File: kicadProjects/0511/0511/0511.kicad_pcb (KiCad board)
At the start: 2 copper layers, 527.5 x 359.5 mm, 377 parts, among them J1 USB4120-03-C_REVA6, U5 UDA1334A_Breakout, U6 STM32F411RETx, U7 BD33HC5WEFJ-E2, Y1 32.768KHz, Y2 8MHz

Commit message: poursuite annotaion circuits rdc
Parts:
- moved MCP23017_ADD20 351.1 mm to (213.3, 251.2)
- moved B0_21_C1 268.0 mm to (162.5, 208.3)
- moved A0_20_C1 265.9 mm to (164.7, 223.5)
- moved B0_21_D1 265.9 mm to (164.8, 215.9)
- moved MCP23017_ADD21 50.1 mm to (212.7, 280.5)
- moved MCP23017_ADD22 49.7 mm to (213.7, 225.9)
- moved R131 16.2 mm to (244.3, 344.3)
- moved R132 16.2 mm to (244.3, 346.8)
- moved CR1 16.2 mm to (244.9, 341.5)
- moved B6_20_D1 15.5 mm to (176.5, 190.0)
- moved B6_20_R1 7.76 mm to (183.3, 190.0)
- renumbered C11 to A0_20_C1, D7 to A0_20_D1, R28 to A0_20_R1, R29 to A0_20_R2, C28 to A0_21_C1, D24 to A0_21_D2, R63 to A0_21_R1, R62 to A0_21_R2, C43 to A0_22_C1, D39 to A0_22_D1, R93 to A0_22_R1, R92 to A0_22_R2, A0_23 to A0_4, C10 to A1_20_C1, D6 to A1_20_D1, R26 to A1_20_R1, R27 to A1_20_R2, C27 to A1_21_C1, D23 to A1_21_D1, R61 to A1_21_R1, R60 to A1_21_R2, C42 to A1_22_C1, D38 to A1_22_D1, R91 to A1_22_R1, R90 to A1_22_R2, A1_23 to A1_4, C9 to A2_20_C1, D5 to A2_20_D1, R25 to A2_20_R1, R24 to A2_20_R2, C26 to A2_21_C1, D22 to A2_21_D1, R59 to A2_21_R1, R58 to A2_21_R2, C41 to A2_22_C1, D37 to A2_22_D1, R89 to A2_22_R1, R88 to A2_22_R2, A2_23 to A2_4, C20 to A3_20_C1, D16 to A3_20_D1, R47 to A3_20_R1, R46 to A3_20_R2, C21 to A3_21_C1, D17 to A3_21_D1, R49 to A3_21_R1, R48 to A3_21_R2, C52 to A3_22_C1, D48 to A3_22_D1, R111 to A3_22_R1, R110 to A3_22_R2, A3_23 to A3_4, C69 to A4_20_C1, D65 to A4_20_D1, R145 to A4_20_R1, R144 to A4_20_R2, C25 to A4_21_C1, D21 to A4_21_D1, R57 to A4_21_R1, R56 to A4_21_R2, C70 to A4_22_C1, D66 to A4_22_D1, R147 to A4_22_R1, R146 to A4_22_R2, A4_23 to A4_4, D3 to A5_20_D1, R21 to A5_20_R1, R20 to A5_20_R2, C23 to A5_21_C1, D19 to A5_21_D1, R53 to A5_21_R1, R52 to A5_21_R2, C39 to A5_22_C1, D35 to A5_22_D1, R85 to A5_22_R1, R84 to A5_22_R2, A5_23 to A5_4, C6 to A6_20_C1, D2 to A6_20_D1, R19 to A6_20_R1, R18 to A6_20_R2, C22 to A6_21_C1, D18 to A6_21_D1, R51 to A6_21_R1, R50 to A6_21_R2, C38 to A6_22_C1, D34 to A6_22_D1, R83 to A6_22_R1, R82 to A6_22_R2, A6_23 to A6_4, C12 to A7_20_C1, D8 to A7_20_D1, R31 to A7_20_R1, R30 to A7_20_R2, C36 to A7_21_C1, D32 to A7_21_D1, R79 to A7_21_R1, R78 to A7_21_R2, C44 to A7_22_C1, D40 to A7_22_D1, R95 to A7_22_R1, R94 to A7_22_R2, A7_23 to A7_4, C18 to B0_20_C1, D14 to B0_20_D1, R43 to B0_20_R1, R42 to B0_20_R2, C35 to B0_21_C1, D31 to B0_21_D1, R76 to B0_21_R1, R77 to B0_21_R2, C51 to B0_22_C1, D47 to B0_22_D1, R109 to B0_22_R1, R108 to B0_22_R2, B0_23 to B0_4, C17 to B1_20_C1, D13 to B1_20_D1, R41 to B1_20_R1, R40 to B1_20_R2, D30 to B1_21_D1, R75 to B1_21_R1, R74 to B1_21_R2, C50 to B1_22_C1, D46 to B1_22_D1, R107 to B1_22_R1, R106 to B1_22_R2, B1_23 to B1_4, C16 to B2_20_C1, D12 to B2_20_D1, R38 to B2_20_R1, R39 to B2_20_R2, C33 to B2_21_C1, D29 to B2_21_D1, R72 to B2_21_R1, R73 to B2_21_R2, C49 to B2_22_C1, D45 to B2_22_D1, R105 to B2_22_R1, R104 to B2_22_R2, B2_23 to B2_4, C15 to B3_20_C1, D11 to B3_20_D1, R37 to B3_20_R1, R36 to B3_20_R2, C32 to B3_21_C1, D28 to B3_21_D1, R71 to B3_21_R1, R70 to B3_21_R2, C48 to B3_22_C1, D44 to B3_22_D1, R103 to B3_22_R1, R102 to B3_22_R2, B3_23 to B3_4, C14 to B4_20_C1, D10 to B4_20_D1, R34 to B4_20_R1, R35 to B4_20_R2, C31 to B4_21_C1, D27 to B4_21_D1, R69 to B4_21_R1, R68 to B4_21_R2, C47 to B4_22_C1, D43 to B4_22_D1, R101 to B4_22_R1, R100 to B4_22_R2, B4_23 to B4_4, C13 to B5_20_C1, D9 to B5_20_D1, R33 to B5_20_R1, R32 to B5_20_R2, C30 to B5_21_C1, D26 to B5_21_D1, R67 to B5_21_R1, R66 to B5_21_R2, C46 to B5_22_C1, D42 to B5_22_D1, R99 to B5_22_R1, R98 to B5_22_R2, B5_23 to B5_4, C88 to B6_20_C1, D70 to B6_20_D1, R154 to B6_20_R1, R155 to B6_20_R2, C37 to B6_21_C1, D33 to B6_21_D1, R81 to B6_21_R1, R80 to B6_21_R2, C53 to B6_22_C1, D49 to B6_22_D1, R113 to B6_22_R1, R112 to B6_22_R2, B6_23 to B6_4, C19 to B7_20_C1, D15 to B7_20_D1, R45 to B7_20_R1, R44 to B7_20_R2, C29 to B7_21_C1, D25 to B7_21_D1, R65 to B7_21_R1, R64 to B7_21_R2, C45 to B7_22_C1, D41 to B7_22_D1, R97 to B7_22_R1, R96 to B7_22_R2, BTN_NRST_STM32 to BTN_NRST_STM1, C34 to C27, C54 to C45, C55 to C46, C57 to C47, C58 to C48, C59 to C49, C60 to C50, C61 to C51, C62 to C52, C63 to C53, C64 to C54, C65 to C55, C66 to C56, C67 to C57, C68 to C58, C71 to C61, C72 to C62, C73 to C63, C74 to C64, C75 to C65, C76 to C66, C77 to C67, C78 to C68, C79 to C69, C80 to C70, C81 to C71, C82 to C72, C83 to C73, C84 to C74, C85 to C75, C86 to C76, C87 to C77, D50 to D41, D51 to D42, D53 to D43, D54 to D44, D55 to D45, D56 to D46, D57 to D47, D58 to D48, D59 to D49, D60 to D50, D61 to D51, D62 to D52, D63 to D53, D64 to D54, D67 to D57, D68 to D58, D69 to D59, MCP23017_ADD23 to MCP23017_AD23, R120 to R100, R121 to R101, R122 to R102, R123 to R103, R124 to R104, R125 to R105, R126 to R106, R127 to R107, R128 to R108, R129 to R109, R130 to R110, R131 to R111, R132 to R112, R133 to R113, R134 to R114, R135 to R115, R136 to R116, R137 to R117, R138 to R118, R139 to R119, R140 to R120, R141 to R121, R142 to R122, R143 to R123, R148 to R128, R149 to R129, R150 to R130, R151 to R131, R152 to R132, R153 to R133, R114 to R96, R115 to R97, R116 to R98, R117 to R99, U5 to U1, U6 to U2, U7 to U3

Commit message: fin annotation bouttons
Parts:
- moved B0_20_R2 367.0 mm to (202.7, 177.0)
- moved B0_20_R1 315.1 mm to (194.7, 177.0)
- moved B0_22_R1 282.4 mm to (194.3, 233.5)
- moved B0_22_R2 271.3 mm to (202.5, 233.5)
- moved B0_22_D1 261.8 mm to (185.5, 233.5)
- moved B0_22_C1 247.2 mm to (210.2, 233.5)
- moved B0_20_D1 190.7 mm to (186.4, 177.3)
- moved B1_21_C1 159.6 mm to (443.2, 317.0)
- moved B0_20_C1 159.5 mm to (211.7, 177.0)
- moved MCP23017_ADD20 65.8 mm to (220.2, 185.7)
- moved MCP23017_ADD21 65.8 mm to (219.5, 215.0)
- moved MCP23017_AD23 63.8 mm to (219.3, 266.1)
- moved B0_21_D1 21.7 mm to (144.4, 223.2)
- moved MCP23017_ADD22 17.0 mm to (219.7, 241.8)
- moved B0_21_C1 16.2 mm to (155.7, 223.0)
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- renumbered A0_4 to A0_23, C49 to A0_23_C1, D45 to A0_23_D1, R105 to A0_23_R1, R104 to A0_23_R2, A1_4 to A1_23, C48 to A1_23_C1, D44 to A1_23_D1, R103 to A1_23_R1, R102 to A1_23_R2, A2_4 to A2_23, C47 to A2_23_C1, D43 to A2_23_D1, R101 to A2_23_R1, R100 to A2_23_R2, A3_4 to A3_23, C57 to A3_23_C1, D53 to A3_23_D1, R121 to A3_23_R1, R120 to A3_23_R2, A4_4 to A4_23, C61 to A4_23_C1, D57 to A4_23_D1, R129 to A4_23_R1, R128 to A4_23_R2, A5_4 to A5_23, C46 to A5_23_C1, D42 to A5_23_D1, R99 to A5_23_R1, R98 to A5_23_R2, A6_4 to A6_23, C45 to A6_23_C1, D41 to A6_23_D1, R97 to A6_23_R1, R96 to A6_23_R2, A7_4 to A7_23, C50 to A7_23_C1, D46 to A7_23_D1, R107 to A7_23_R1, R106 to A7_23_R2, B0_4 to B0_23, C56 to B0_23_C1, D52 to B0_23_D1, R119 to B0_23_R1, R118 to B0_23_R2, C27 to B1_21_C1, B1_4 to B1_23, C55 to B1_23_C1, D51 to B1_23_D1, R117 to B1_23_R1, R116 to B1_23_R2, B2_4 to B2_23, C54 to B2_23_C1, D50 to B2_23_D1, R115 to B2_23_R1, R114 to B2_23_R2, B3_4 to B3_23, C53 to B3_23_C1, D49 to B3_23_D1, R113 to B3_23_R1, R112 to B3_23_R2, B4_4 to B4_23, C52 to B4_23_C1, D48 to B4_23_D1, R111 to B4_23_R1, R110 to B4_23_R2, B5_4 to B5_23, C51 to B5_23_C1, D47 to B5_23_D1, R109 to B5_23_R1, R108 to B5_23_R2, B6_4 to B6_23, C58 to B6_23_C1, D54 to B6_23_D1, R123 to B6_23_R1, R122 to B6_23_R2, C2 to C_DECOUPLAGE_20, C4 to C_DECOUPLAGE_21, C3 to C_DECOUPLAGE_22, C1 to C_DECOUPLAGE_23, R9 to PULLUP_INTB_20, R12 to PULLUP_INTB_21, R8 to PULLUP_INTB_22, R2 to PULLUP_INTB_23, R3 to PULLUP_INT_20, R14 to PULLUP_INT_21, R5 to PULLUP_INT_22, R1 to PULLUP_INT_23, R11 to RESET_PULLUP_20, R13 to RESET_PULLUP_21, R10 to RESET_PULLUP_22, R4 to RESET_PULLUP_23

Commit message: fin placement mcp23017 addresse 20
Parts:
- moved B2_20_D1 390.6 mm to (176.7, 179.5)
- moved B1_20_R2 364.3 mm to (203.7, 175.0)
- moved B2_20_C1 350.3 mm to (212.7, 180.5)
- moved B7_20_R1 349.8 mm to (195.5, 195.5)
- moved B3_20_D1 349.1 mm to (184.5, 183.5)
- moved A5_20_R2 341.3 mm to (243.0, 175.5)
- moved B7_20_D1 340.4 mm to (183.3, 195.0)
- moved B3_20_R1 338.9 mm to (195.5, 184.0)
- moved B4_20_D1 338.4 mm to (176.6, 186.5)
- moved B1_20_R1 333.0 mm to (194.5, 175.0)
- moved A2_20_C1 329.5 mm to (228.0, 183.5)
- moved A1_20_R2 328.2 mm to (243.2, 184.5)
- moved B5_20_R2 321.3 mm to (206.2, 188.5)
- moved B3_20_C1 320.5 mm to (212.7, 182.0)
- moved B7_20_C1 308.8 mm to (212.5, 188.0)
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- renumbered C7 to A5_20_C1
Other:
- board size 527.5 x 359.5 mm -> 527.5 x 278 mm

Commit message: placed left hand buttons
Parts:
- moved A6_23 162.6 mm to (354.0, -75.8)
- moved A6_22 160.8 mm to (395.0, 0.42)
- moved B6_22 147.7 mm to (395.0, -18.6)
- moved B4_23 138.7 mm to (354.0, -18.6)
- moved A4_23 138.5 mm to (354.0, -0.08)
- moved B5_23 136.6 mm to (354.0, -56.7)
- moved B1_23 133.7 mm to (376.0, -18.6)
- moved B6_23 131.0 mm to (354.0, -94.8)
- moved A1_23 127.6 mm to (373.0, -0.08)
- moved B3_23 119.6 mm to (376.0, -94.8)
- moved A0_23 117.7 mm to (394.0, -75.8)
- moved B0_23 116.0 mm to (395.0, -94.8)
- moved A5_23 113.0 mm to (354.0, -37.7)
- moved A3_23 104.6 mm to (376.0, -75.8)
- moved A7_22 98.1 mm to (395.0, -37.7)
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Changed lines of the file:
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@@
 	(footprint "Button_Switch_Keyboard:SW_Cherry_MX_1.00u_PCB"
 		(layer "F.Cu")
-		(at 492.37 -28.17)
+		(at 353.99 -18.63)
 		(descr "Cherry MX keyswitch, 1.00u, PCB mount, http://cherryamericas.com/wp-content/uploads/2014/12/mx_cat.pdf")
 		(tags "Cherry MX keyswitch 1.00u PCB")
@@
 	(footprint "Button_Switch_Keyboard:SW_Cherry_MX_1.00u_PCB"
 		(layer "F.Cu")
-		(at 508.55 -113.49)
+		(at 395.04 0.42)
 		(descr "Cherry MX keyswitch, 1.00u, PCB mount, http://cherryamericas.com/wp-content/uploads/2014/12/mx_cat.pdf")
 		(tags "Cherry MX keyswitch 1.00u PCB")
@@
 	(footprint "Button_Switch_Keyboard:SW_Cherry_MX_1.00u_PCB"
 		(layer "F.Cu")
-		(at 458.19 -28.17)
+		(at 375.99 -37.68)
 		(descr "Cherry MX keyswitch, 1.00u, PCB mount, http://cherryamericas.com/wp-content/uploads/2014/12/mx_cat.pdf")
 		(tags "Cherry MX keyswitch 1.00u PCB")
@@
 	(footprint "Button_Switch_Keyboard:SW_Cherry_MX_1.00u_PCB"
 		(layer "F.Cu")
-		(at 458.19 -11.08)
+		(at 375.99 -75.78)
 		(descr "Cherry MX keyswitch, 1.00u, PCB mount, http://cherryamericas.com/wp-content/uploads/2014/12/mx_cat.pdf")
 		(tags "Cherry MX keyswitch 1.00u PCB")
@@
 	(footprint "Capacitor_SMD:C_0603_1608Metric"
 		(layer "F.Cu")
-		(at 212.275 244.5)
+		(at 272.275 225.965)
 		(descr "Capacitor SMD 0603 (1608 Metric), square (rectangular) end terminal, IPC-7351 nominal, (Body size source: IPC-SM-782 page 76, https://www.pcb-3d.com/wordpress/wp-content/uploads/ipc-sm-782a_amendment_1_and_2.pdf), generated with kicad-footprint-generator")
 		(tags "capacitor")
@@
 	(footprint "Button_Switch_Keyboard:SW_Cherry_MX_1.00u_PCB"
 		(layer "F.Cu")
-		(at 492.37 -45.26)
+		(at 373.04 -0.08)
 		(descr "Cherry MX keyswitch, 1.00u, PCB mount, http://cherryamericas.com/wp-content/uploads/2014/12/mx_cat.pdf")
 		(tags "Cherry MX keyswitch 1.00u PCB")
@@
 	(footprint "Button_Switch_Keyboard:SW_Cherry_MX_1.00u_PCB"
 		(layer "F.Cu")
-		(at 475.28 6.01)
+		(at 353.99 -56.73)
 		(descr "Cherry MX keyswitch, 1.00u, PCB mount, http://cherryamericas.com/wp-content/uploads/2014/12/mx_cat.pdf")
 		(tags "Cherry MX keyswitch 1.00u PCB")
@@
 	(footprint "Button_Switch_Keyboard:SW_Cherry_MX_1.00u_PCB"
 		(layer "F.Cu")
-		(at 509.46 -45.26)
+		(at 473.63 -52.85)
 		(descr "Cherry MX keyswitch, 1.00u, PCB mount, http://cherryamericas.com/wp-content/uploads/2014/12/mx_cat.pdf")
 		(tags "Cherry MX keyswitch 1.00u PCB")
@@
 	(footprint "Button_Switch_Keyboard:SW_Cherry_MX_1.00u_PCB"
 		(layer "F.Cu")
-		(at 475.28 -11.08)
+		(at 395.04 -94.83)
 		(descr "Cherry MX keyswitch, 1.00u, PCB mount, http://cherryamericas.com/wp-content/uploads/2014/12/mx_cat.pdf")
 		(tags "Cherry MX keyswitch 1.00u PCB")
@@
 	(footprint "Button_Switch_Keyboard:SW_Cherry_MX_1.00u_PCB"
 		(layer "F.Cu")
-		(at 509.46 -11.08)
+		(at 375.99 -18.63)
 		(descr "Cherry MX keyswitch, 1.00u, PCB mount, http://cherryamericas.com/wp-content/uploads/2014/12/mx_cat.pdf")
 		(tags "Cherry MX keyswitch 1.00u PCB")
@@
 	(footprint "Button_Switch_Keyboard:SW_Cherry_MX_1.00u_PCB"
 		(layer "F.Cu")
-		(at 474.37 -79.31)
+		(at 395.04 -56.73)
 		(descr "Cherry MX keyswitch, 1.00u, PCB mount, http://cherryamericas.com/wp-content/uploads/2014/12/mx_cat.pdf")
 		(tags "Cherry MX keyswitch 1.00u PCB")
@@
 	(footprint "Button_Switch_Keyboard:SW_Cherry_MX_1.00u_PCB"
 		(layer "F.Cu")
-		(at 491.46 -130.58)
+		(at 395.04 -18.63)
 		(descr "Cherry MX keyswitch, 1.00u, PCB mount, http://cherryamericas.com/wp-content/uploads/2014/12/mx_cat.pdf")
 		(tags "Cherry MX keyswitch 1.00u PCB")
@@
 	(footprint "Button_Switch_Keyboard:SW_Cherry_MX_1.00u_PCB"
 		(layer "F.Cu")
-		(at 475.28 -45.26)
+		(at 353.99 -94.83)
 		(descr "Cherry MX keyswitch, 1.00u, PCB mount, http://cherryamericas.com/wp-content/uploads/2014/12/mx_cat.pdf")
 		(tags "Cherry MX keyswitch 1.00u PCB")
@@
 	(footprint "Button_Switch_Keyboard:SW_Cherry_MX_1.00u_PCB"
 		(layer "F.Cu")
-		(at 458.19 6.01)
+		(at 353.99 -37.68)
 		(descr "Cherry MX keyswitch, 1.00u, PCB mount, http://cherryamericas.com/wp-content/uploads/2014/12/mx_cat.pdf")
 		(tags "Cherry MX keyswitch 1.00u PCB")
@@
 	(footprint "Button_Switch_Keyboard:SW_Cherry_MX_1.00u_PCB"
 		(layer "F.Cu")
-		(at 648.96 174.42)
+		(at 648.54 206.42)
 		(descr "Cherry MX keyswitch, 1.00u, PCB mount, http://cherryamericas.com/wp-content/uploads/2014/12/mx_cat.pdf")
 		(tags "Cherry MX keyswitch 1.00u PCB")
@@
 	(footprint "Button_Switch_Keyboard:SW_Cherry_MX_1.00u_PCB"
 		(layer "F.Cu")
-		(at 475.28 -28.17)
+		(at 375.99 -94.83)
 		(descr "Cherry MX keyswitch, 1.00u, PCB mount, http://cherryamericas.com/wp-content/uploads/2014/12/mx_cat.pdf")
 		(tags "Cherry MX keyswitch 1.00u PCB")
@@
 	(footprint "Button_Switch_Keyboard:SW_Cherry_MX_1.00u_PCB"
 		(layer "F.Cu")
-		(at 492.37 6.01)
+		(at 353.99 -0.08)
 		(descr "Cherry MX keyswitch, 1.00u, PCB mount, http://cherryamericas.com/wp-content/uploads/2014/12/mx_cat.pdf")
 		(tags "Cherry MX keyswitch 1.00u PCB")
@@
 	(footprint "Button_Switch_Keyboard:SW_Cherry_MX_1.00u_PCB"
 		(layer "F.Cu")
-		(at 492.37 -11.08)
+		(at 394.04 -75.78)
 		(descr "Cherry MX keyswitch, 1.00u, PCB mount, http://cherryamericas.com/wp-content/uploads/2014/12/mx_cat.pdf")
 		(tags "Cherry MX keyswitch 1.00u PCB")
@@
 	(footprint "Button_Switch_Keyboard:SW_Cherry_MX_1.00u_PCB"
 		(layer "F.Cu")
-		(at 509.46 -28.17)
+		(at 353.99 -75.78)
 		(descr "Cherry MX keyswitch, 1.00u, PCB mount, http://cherryamericas.com/wp-content/uploads/2014/12/mx_cat.pdf")
 		(tags "Cherry MX keyswitch 1.00u PCB")
@@
 	(footprint "Button_Switch_Keyboard:SW_Cherry_MX_1.00u_PCB"
 		(layer "F.Cu")
-		(at 458.19 -45.26)
+		(at 375.99 -56.73)
 		(descr "Cherry MX keyswitch, 1.00u, PCB mount, http://cherryamericas.com/wp-content/uploads/2014/12/mx_cat.pdf")
 		(tags "Cherry MX keyswitch 1.00u PCB")
@@
 	(footprint "Button_Switch_Keyboard:SW_Cherry_MX_1.00u_PCB"
 		(layer "F.Cu")
-		(at 457.28 -113.49)
+		(at 395.04 -37.68)
 		(descr "Cherry MX keyswitch, 1.00u, PCB mount, http://cherryamericas.com/wp-content/uploads/2014/12/mx_cat.pdf")
 		(tags "Cherry MX keyswitch 1.00u PCB")

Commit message: added script to place components
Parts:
- moved B7_21_R2 387.1 mm to (195.0, 216.5)
- moved A7_23_C1 367.2 mm to (230.0, 266.5)
- moved B1_21_R1 354.8 mm to (200.0, 207.5)
- moved B3_21_R1 354.3 mm to (200.0, 210.5)
- moved A7_23_D1 353.7 mm to (235.0, 266.5)
- moved B3_21_R2 352.6 mm to (195.0, 210.5)
- moved B4_21_R1 349.7 mm to (200.0, 212.0)
- moved B5_22_D1 349.2 mm to (205.0, 240.5)
- moved B5_22_C1 345.6 mm to (210.0, 240.5)
- moved A6_22_C1 345.6 mm to (230.0, 242.0)
- moved A0_23_C1 344.1 mm to (230.0, 256.0)
- moved A6_22_D1 334.4 mm to (235.0, 242.0)
- moved A3_23_C1 333.7 mm to (230.0, 260.5)
- moved A7_21_C1 330.7 mm to (230.0, 216.5)
- moved A0_23_D1 330.6 mm to (235.0, 256.0)
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
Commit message: poursuite placement
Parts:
- removed A0_21_D2: D_Schottky, Diode_SMD:D_SOD-123
- added A0_21_D1: D_Schottky, Diode_SMD:D_SOD-123, F.Cu at (173.9, 222.6)
- moved C75 483.3 mm to (102.5, 45.5)
- moved C74 477.6 mm to (102.2, 55.0)
- moved C76 475.9 mm to (110.3, 49.5)
- moved BTN_NRST_STM1 449.9 mm to (201.0, 159.9)
- moved PULLUP_INTB_21 403.9 mm to (166.3, 238.6)
- moved RESET_PULLUP_21 401.6 mm to (166.6, 236.1)
- moved Y2 388.0 mm to (148.0, 161.4)
- moved C77 384.4 mm to (162.3, 153.4)
- moved D1 375.7 mm to (176.5, 104.9)
- moved 4.7uF1 367.2 mm to (161.0, 174.4)
- moved RESET_PULLUP_20 360.6 mm to (169.3, 205.1)
- moved PULLUP_INTB_20 351.0 mm to (169.3, 209.6)
- moved C5 350.2 mm to (194.1, 104.4)
- moved RESET_PULLUP_22 342.4 mm to (170.4, 263.1)
- moved R16 339.2 mm to (189.5, 104.4)
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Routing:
- net GND: track 140.4 -> 0.00 mm
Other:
- board size 527.5 x 278 mm -> 273.5 x 278 mm

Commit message: ajouut ferrite
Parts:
- added C1: 100nF, Capacitor_SMD:C_0603_1608Metric, F.Cu at (148.2, 165.0)
- added FB1: FerriteBead, Inductor_SMD:L_0603_1608Metric, F.Cu at (148.2, 167.5)
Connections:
- U2 pad 13: +3.3V -> Net-(U2-VDDA)

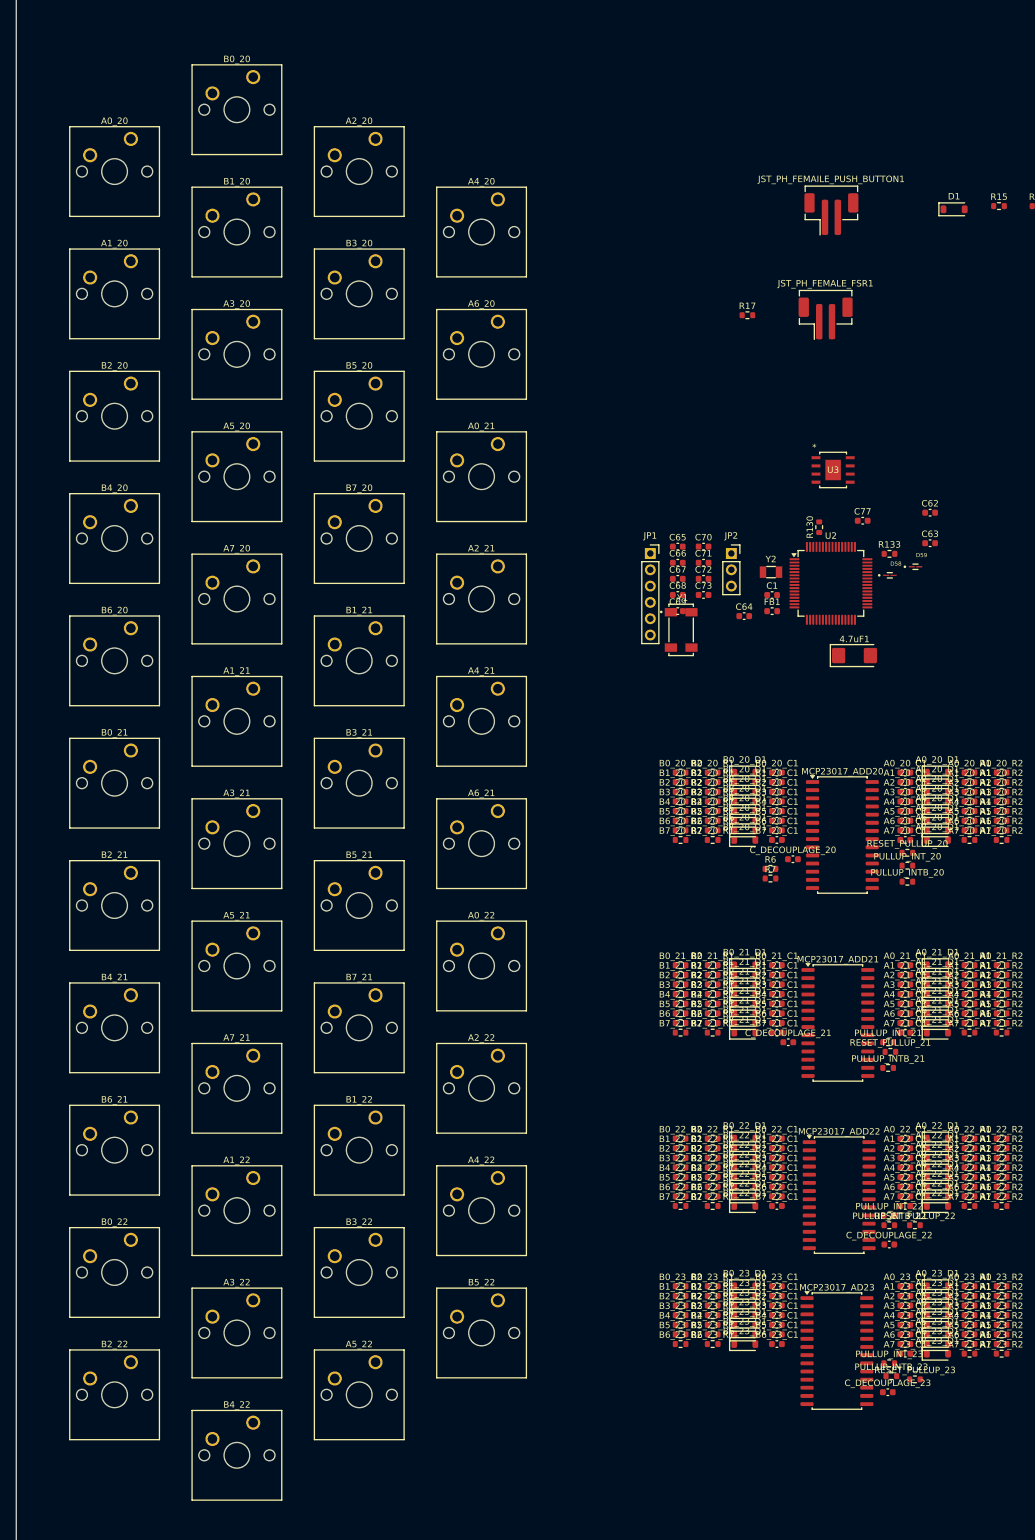
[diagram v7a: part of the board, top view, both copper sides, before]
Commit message: placed D1 and R1 and for right hand
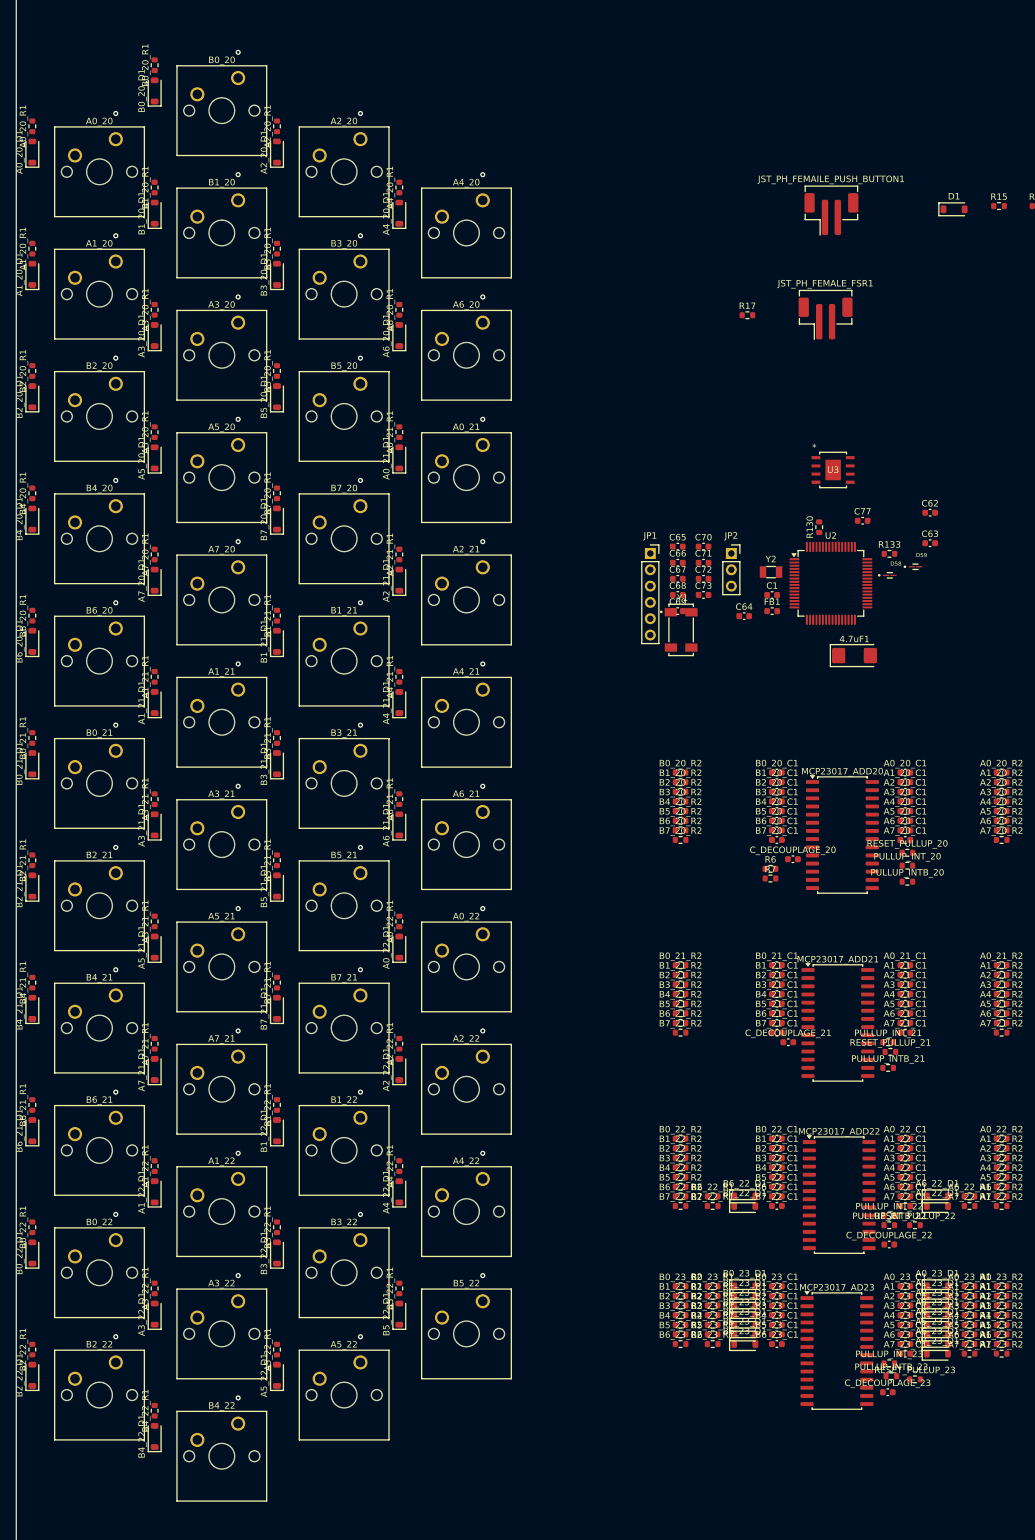
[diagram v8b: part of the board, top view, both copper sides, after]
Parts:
- moved A0_20_R1 177.3 mm to (33.0, 92.0), turned to 90 degrees
- moved A0_20_D1 170.9 mm to (33.0, 96.0), turned to 90 degrees
- moved A1_20_R1 167.9 mm to (33.0, 111.0), turned to 90 degrees
- moved A1_20_D1 161.6 mm to (33.0, 115.0), turned to 90 degrees
- moved A2_20_R1 149.6 mm to (71.1, 92.0), turned to 90 degrees
- moved A3_20_R1 148.2 mm to (52.0, 120.6), turned to 90 degrees
- moved A2_20_D1 143.2 mm to (71.1, 96.0), turned to 90 degrees
- moved A3_20_D1 141.9 mm to (52.0, 124.6), turned to 90 degrees
- moved A5_20_R1 140.6 mm to (52.0, 139.6), turned to 90 degrees
- moved B0_20_D1 140.4 mm to (52.0, 86.5), turned to 90 degrees
- moved B0_20_R1 140.3 mm to (52.0, 82.5), turned to 90 degrees
- moved A1_21_R1 135.1 mm to (52.0, 177.7), turned to 90 degrees
- moved A7_20_R1 134.5 mm to (52.0, 158.7), turned to 90 degrees
- moved A5_20_D1 134.4 mm to (52.0, 143.6), turned to 90 degrees
- moved A4_20_R1 131.6 mm to (90.2, 101.5), turned to 90 degrees
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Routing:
- net GND: vias 0 -> 44
